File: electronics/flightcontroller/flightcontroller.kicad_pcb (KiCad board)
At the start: 4 copper layers, 30 x 50 mm, 80 parts, among them J1 BAT+, J10 USB, J11 Payload, J12 BAT-, J13 Conn_01x04, J2 ESC+, J3 ESC, J4 Servo3, J5 Servo2, J6 Servo1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

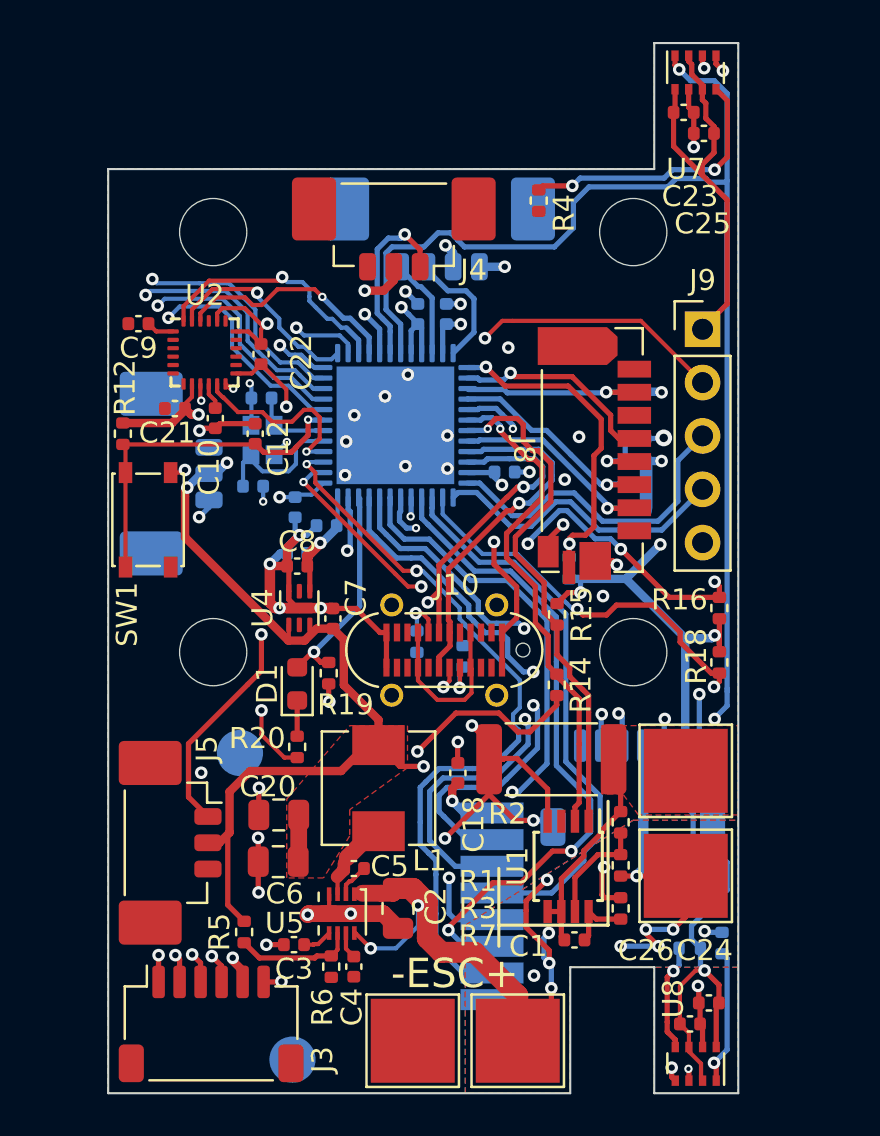
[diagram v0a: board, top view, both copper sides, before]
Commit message: electronics: Fixed most flightcontroller DRC errors.
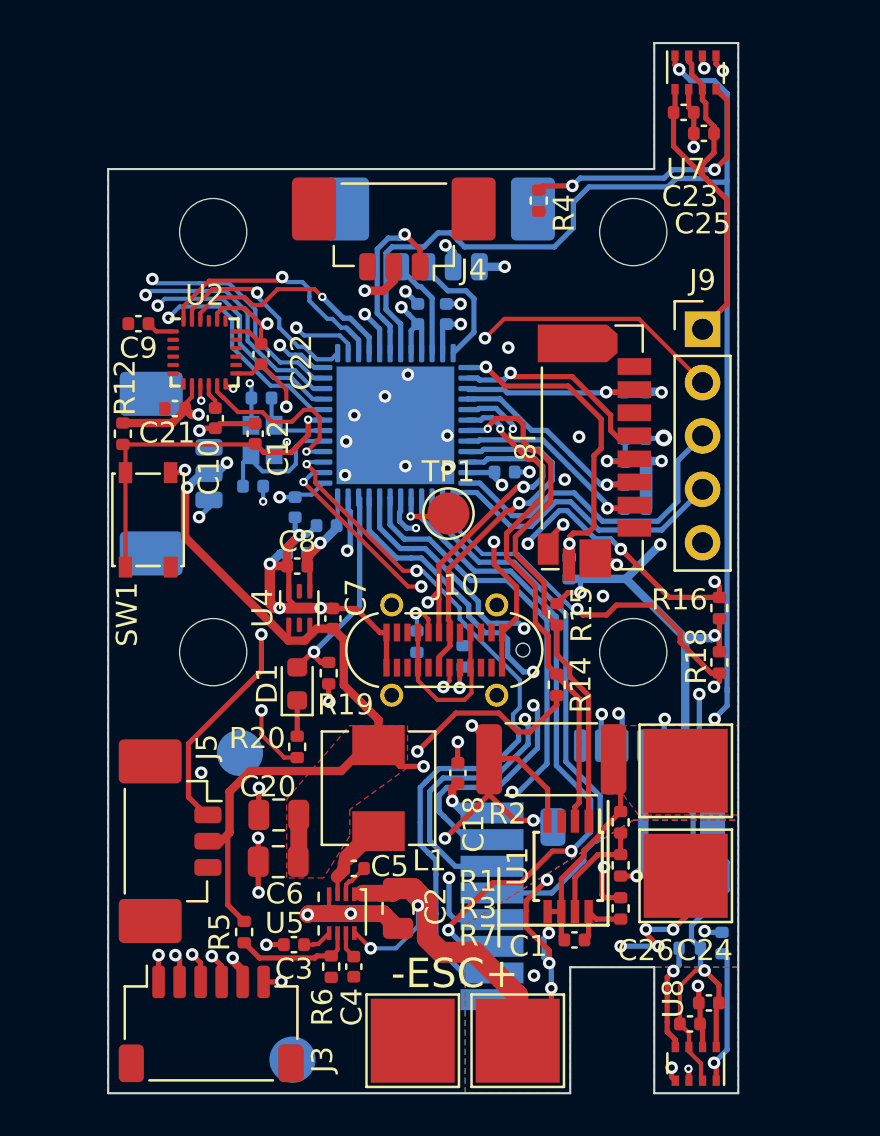
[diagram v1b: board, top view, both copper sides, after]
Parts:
- added TP1: SWO, TestPoint:TestPoint_Pad_D2.0mm, F.Cu at (201.2, 83.4)
- moved J8 0.12 mm to (208.5, 80.2)
- moved J5 0.08 mm to (188.5, 99.0)
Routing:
- net /MCU/SWO: track 0.91 -> 2.77 mm
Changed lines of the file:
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@@
   )
   (footprint "flightcontroller-footprints:HYC80-TF08-XXX" (layer "F.Cu")
-    (at 208.5 80.375 -90)
+    (at 208.5 80.25 -90)
     (property "Sheetfile" "mcu.kicad_sch")
     (property "Sheetname" "MCU")
@@
   )
   (footprint "Connector_Molex:Molex_PicoBlade_53398-0371_1x03-1MP_P1.25mm_Vertical" (layer "F.Cu")
-    (at 188.5 99.075 -90)
+    (at 188.5 99 -90)
     (descr "Molex PicoBlade series connector, 53398-0371 (http://www.molex.com/pdm_docs/sd/533980271_sd.pdf), generated with kicad-footprint-generator")
     (tags "connector Molex PicoBlade side entry")
@@
     )
   )
+  (footprint "TestPoint:TestPoint_Pad_D2.0mm" (layer "F.Cu")
+    (at 201.2 83.4)
+    (descr "SMD pad as test Point, diameter 2.0mm")
+    (tags "test point SMD pad")
+    (property "Sheetfile" "mcu.kicad_sch")
+    (property "Sheetname" "MCU")
+    (attr exclude_from_pos_files)
+    (fp_text reference "TP1" (at 0 -1.998) (layer "F.SilkS")
+      (effects (font (size 1 1) (thickness 0.15)))
+    )
+    (fp_text value "SWO" (at 0 2.05) (layer "F.Fab")
+      (effects (font (size 1 1) (thickness 0.15)))
+    )
+    (fp_text user "${REFERENCE}" (at 0 -2) (layer "F.Fab")
+      (effects (font (size 1 1) (thickness 0.15)))
+    )
+    (fp_circle (center 0 0) (end 0 1.2) (layer "F.SilkS") (width 0.12) (fill none))
+    (fp_circle (center 0 0) (end 1.5 0) (layer "F.CrtYd") (width 0.05) (fill none))
+    (pad "1" smd circle locked (at 0 0) (size 2 2) (layers "F.Cu" "F.Mask")
+      (net 39 "/MCU/SWO") (pinfunction "1") (pintype "passive"))
+  )
   (footprint "Capacitor_SMD:C_0402_1005Metric" (layer "F.Cu")
     (at 192.278 75.808 90)
@@
   (segment (start 196.925 82.6375) (end 196.97548 82.68798) (width 0.25) (layer "B.Cu") (net 38))
   (segment (start 196.97548 83.1) (end 196.975481 84.399623) (width 0.25) (layer "B.Cu") (net 38))
+  (segment (start 199.4005 83.54) (end 201.06 83.54) (width 0.25) (layer "F.Cu") (net 39))
+  (segment (start 201.06 83.54) (end 201.2 83.4) (width 0.25) (layer "F.Cu") (net 39))
   (via (at 199.4005 83.54) (size 0.4) (drill 0.2) (layers "F.Cu" "B.Cu") (net 39))
   (segment (start 199.425 83.5155) (end 199.4005 83.54) (width 0.25) (layer "B.Cu") (net 39))
@@
   (segment (start 209.545 77.62) (end 209.565 77.6) (width 0.25) (layer "B.Cu") (net 48))
   (segment (start 208.71 77.62) (end 209.545 77.62) (width 0.25) (layer "B.Cu") (net 48))
-  (segment (start 208.125489 84.035) (end 207.73 84.430489) (width 0.25) (layer "F.Cu") (net 49))
-  (segment (start 208.125489 80.641318) (end 208.125489 84.035) (width 0.25) (layer "F.Cu") (net 49))
-  (segment (start 208.475969 80.290838) (end 208.125489 80.641318) (width 0.25) (layer "F.Cu") (net 49))
-  (segment (start 208.475969 78.90488) (end 208.475969 80.290838) (width 0.25) (layer "F.Cu") (net 49))
-  (segment (start 207.73 84.430489) (end 207.115489 84.430489) (width 0.25) (layer "F.Cu") (net 49))
-  (segment (start 206.901089 77.33) (end 208.475969 78.90488) (width 0.25) (layer "F.Cu") (net 49))
-  (segment (start 202.985569 76.419849) (end 203.89572 77.33) (width 0.25) (layer "F.Cu") (net 49))
+  (segment (start 206.96 84.520978) (end 207.150978 84.33) (width 0.25) (layer "F.Cu") (net 49))
+  (segment (start 207.830489 84.33) (end 208.125489 84.035) (width 0.25) (layer "F.Cu") (net 49))
+  (segment (start 206.96 84.83854) (end 206.96 84.520978) (width 0.25) (layer "F.Cu") (net 49))
+  (segment (start 207.150978 84.33) (end 207.830489 84.33) (width 0.25) (layer "F.Cu") (net 49))
+  (segment (start 208.475969 80.290838) (end 208.475969 78.90488) (width 0.25) (layer "F.Cu") (net 49))
+  (segment (start 208.475969 78.90488) (end 206.901089 77.33) (width 0.25) (layer "F.Cu") (net 49))
+  (segment (start 206.901089 77.33) (end 203.89572 77.33) (width 0.25) (layer "F.Cu") (net 49))
+  (segment (start 208.125489 84.035) (end 208.125489 80.641318) (width 0.25) (layer "F.Cu") (net 49))
   (segment (start 206.94 84.85854) (end 206.96 84.83854) (width 0.25) (layer "F.Cu") (net 49))
-  (segment (start 207.115489 84.430489) (end 206.96 84.585978) (width 0.25) (layer "F.Cu") (net 49))
+  (segment (start 203.89572 77.33) (end 202.985569 76.419849) (width 0.25) (layer "F.Cu") (net 49))
   (segment (start 206.94 85.965) (end 206.94 84.85854) (width 0.25) (layer "F.Cu") (net 49))
-  (segment (start 206.96 84.83854) (end 206.96 84.585978) (width 0.25) (layer "F.Cu") (net 49))
-  (segment (start 203.89572 77.33) (end 206.901089 77.33) (width 0.25) (layer "F.Cu") (net 49))
+  (segment (start 208.125489 80.641318) (end 208.475969 80.290838) (width 0.25) (layer "F.Cu") (net 49))
   (via (at 206.96 84.83854) (size 0.6) (drill 0.3) (layers "F.Cu" "B.Cu") (net 49))
   (via (at 202.985569 76.419849) (size 0.6) (drill 0.3) (layers "F.Cu" "B.Cu") (net 49))
@@
   (segment (start 202.1125 76.45) (end 202.955418 76.45) (width 0.25) (layer "B.Cu") (net 49))
   (segment (start 206.95 85.49) (end 206.95 84.84854) (width 0.25) (layer "B.Cu") (net 49))
+  (segment (start 210.265489 74.130489) (end 203.859959 74.130489) (width 0.2) (layer "F.Cu") (net 50))
   (segment (start 185.825 80.235) (end 185.7 80.11) (width 0.2) (layer "F.Cu") (net 50))
-  (segment (start 204.264511 74.225489) (end 203.764959 74.225489) (width 0.2) (layer "F.Cu") (net 50))
+  (segment (start 213.3 77.165) (end 210.265489 74.130489) (width 0.2) (layer "F.Cu") (net 50))
   (segment (start 193.713067 80.486933) (end 192.406933 80.486933) (width 0.25) (layer "F.Cu") (net 50))
-  (segment (start 203.764959 74.225489) (end 202.940621 75.049827) (width 0.2) (layer "F.Cu") (net 50))
-  (segment (start 213.3 77.165) (end 210.360489 74.225489) (width 0.2) (layer "F.Cu") (net 50))
   (segment (start 192.03 80.11) (end 185.7 80.11) (width 0.2) (layer "F.Cu") (net 50))
+  (segment (start 203.859959 74.130489) (end 202.940621 75.049827) (width 0.2) (layer "F.Cu") (net 50))
   (segment (start 185.825 85.95) (end 185.825 81.45) (width 0.2) (layer "F.Cu") (net 50))
   (segment (start 192.406933 80.486933) (end 192 80.08) (width 0.25) (layer "F.Cu") (net 50))
@@
   (segment (start 194.52 79.670435) (end 193.945098 80.245337) (width 0.25) (layer "F.Cu") (net 50))
   (segment (start 185.825 81.45) (end 185.825 80.235) (width 0.2) (layer "F.Cu") (net 50))
-  (segment (start 210.360489 74.225489) (end 204.264511 74.225489) (width 0.2) (layer "F.Cu") (net 50))
   (segment (start 193.945098 80.254902) (end 193.713067 80.486933) (width 0.25) (layer "F.Cu") (net 50))
   (segment (start 193.945098 80.245337) (end 193.945098 80.254902) (width 0.25) (layer "F.Cu") (net 50))
@@
   (zone (net 53) (net_name "+BATT") (layers "F.Cu" "In1.Cu" "B.Cu") (hatch edge 0.508)
     (priority 1)
-    (connect_pads yes (clearance 0.508))
+    (connect_pads yes (clearance 0.254))
     (min_thickness 0.254) (filled_areas_thickness no)
     (fill yes (thermal_gap 0.508) (thermal_bridge_width 0.508))
@@
   (zone (net 12) (net_name "/Power Management/-BATT") (layer "F.Cu") (hatch edge 0.508)
     (priority 1)
-    (connect_pads yes (clearance 0.508))
+    (connect_pads yes (clearance 0.254))
     (min_thickness 0.254) (filled_areas_thickness no)
     (fill yes (thermal_gap 0.508) (thermal_bridge_width 0.508))

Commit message: electronics: Add a resistor for ESC power and some test pads.
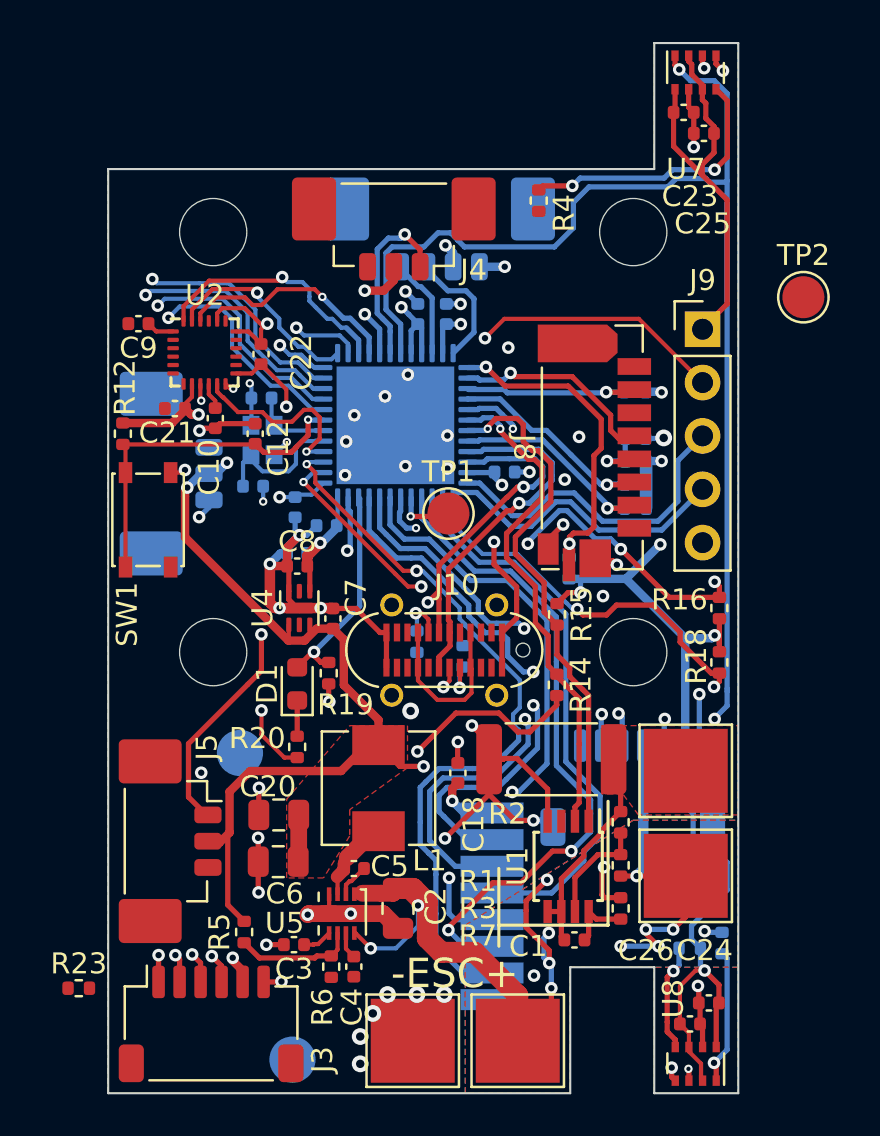
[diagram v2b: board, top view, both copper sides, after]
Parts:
- added R23: DNP, Resistor_SMD:R_0402_1005Metric, F.Cu at (183.6, 106.0)
- added TP2: DAT1, TestPoint:TestPoint_Pad_D2.0mm, F.Cu at (218.1, 73.1)
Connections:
- C9 pad 1: Net-(C9-Pad1) -> +3V3
- J3 pad 5: +3V3 -> Net-(J3-Pad5)
- J8 pad 8: unconnected-(J8-Pad8) -> Net-(J8-Pad8)
- U2 pad 1: Net-(C9-Pad1) -> +3V3
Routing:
- net Net-(C9-Pad1): track 1.32 -> 0.00 mm
- net +3V3: track 212.8 -> 214.2 mm
- net GND: vias 48 -> 55

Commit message: electronics: Placed missing resistors and fixed remaining DRC errors.
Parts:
- added R24: 47k, Resistor_SMD:R_0402_1005Metric, B.Cu at (210.1, 76.4)
- added R25: 47k, Resistor_SMD:R_0402_1005Metric, B.Cu at (210.1, 84.2)
- moved TP2 12.1 mm to (206.0, 72.4)
- moved R23 8.31 mm to (191.5, 103.4), turned to 90 degrees
- moved R5 1.52 mm to (192.0, 101.9), turned to 0 degrees
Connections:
- J8 pad 1: unconnected-(J8-Pad1) -> Net-(J8-Pad1)
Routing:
- net Net-(J8-Pad8): track 0.00 -> 8.70 mm, vias 0 -> 3
- net GND: track 117.7 -> 124.1 mm, vias 55 -> 56
- net +3V3: track 214.2 -> 220.3 mm
- net unconnected-(J10-PadS1): track 11.8 -> 16.2 mm, vias 0 -> 1
- net /MCU/SWDIO: track 15.6 -> 17.5 mm
- net /MCU/SWCLK: track 14.5 -> 16.3 mm
- net Net-(J3-Pad5): track 0.00 -> 1.82 mm
- net Net-(J8-Pad1): track 0.00 -> 1.71 mm, vias 0 -> 1
- net Net-(R5-Pad2): track 5.70 -> 6.70 mm
- net +4V: track 79.1 -> 78.2 mm
